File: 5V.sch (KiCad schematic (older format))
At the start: 11 parts

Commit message: LMZ13608 input caps
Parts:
- added C?: 10µ, Capacitors_SMD:C_1210, symbol Device:C
- added C?: 10µ, symbol Device:C
- C?: value 30µ -> 10µ; footprint (none) -> Capacitors_SMD:C_1210; Dielectric X5R/X7R -> X7R; MPN (none) -> GRM32ER71J106KA12L
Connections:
- net GND: now also C?.2, C?.2
- net VIN: now also C?.1, C?.1
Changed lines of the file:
@@
 	1    0    0    -1
 $EndComp
-Wire Wire Line
-	2650 2750 2800 2750
 NoConn ~ 3500 2700
 $Comp
@@
 P 2800 3000
 F 0 "C?" H 2915 3046 50  0000 L CNN
-F 1 "30µ" H 2915 2955 50  0000 L CNN
-F 2 "" H 2838 2850 50  0001 C CNN
+F 1 "10µ" H 2915 2955 50  0000 L CNN
+F 2 "Capacitors_SMD:C_1210" H 2838 2850 50  0001 C CNN
 F 3 "~" H 2800 3000 50  0001 C CNN
-F 4 "X5R/X7R" H 2800 3000 50  0001 C CNN "Dielectric"
+F 4 "X7R" H 2800 3000 50  0001 C CNN "Dielectric"
+F 5 "GRM32ER71J106KA12L" H 2800 3000 50  0001 C CNN "MPN"
 	1    2800 3000
 	1    0    0    -1
@@
 	1    0    0    -1
 $EndComp
-Wire Wire Line
-	2800 3250 2800 3150
 Text HLabel 5900 3300 1    50   Input ~ 0
 VIN
-Text HLabel 2650 2750 0    50   Input ~ 0
+Text HLabel 1950 2750 0    50   Input ~ 0
 VIN
 Text HLabel 5050 3750 0    50   Input ~ 0
@@
 	1    0    0    -1
 $EndComp
+$Comp
+L Device:C C?
+U 1 1 5C709529
+P 2450 3000
+F 0 "C?" H 2565 3046 50  0000 L CNN
+F 1 "10µ" H 2565 2955 50  0000 L CNN
+F 2 "Capacitors_SMD:C_1210" H 2488 2850 50  0001 C CNN
+F 3 "~" H 2450 3000 50  0001 C CNN
+F 4 "X7R" H 2450 3000 50  0001 C CNN "Dielectric"
+F 5 "GRM32ER71J106KA12L" H 2450 3000 50  0001 C CNN "MPN"
+	1    2450 3000
+	1    0    0    -1
+$EndComp
+$Comp
+L Device:C C?
+U 1 1 5C709573
+P 2100 3000
+F 0 "C?" H 2215 3046 50  0000 L CNN
+F 1 "10µ" H 2215 2955 50  0000 L CNN
+F 2 "" H 2138 2850 50  0001 C CNN
+F 3 "~" H 2100 3000 50  0001 C CNN
+F 4 "X7R" H 2100 3000 50  0001 C CNN "Dielectric"
+F 5 "GRM32ER71J106KA12L" H 2100 3000 50  0001 C CNN "MPN"
+	1    2100 3000
+	1    0    0    -1
+$EndComp
+Wire Wire Line
+	1950 2750 2100 2750
+Wire Wire Line
+	2100 2750 2100 2850
+Wire Wire Line
+	2100 2750 2450 2750
+Wire Wire Line
+	2450 2750 2450 2850
+Connection ~ 2100 2750
+Wire Wire Line
+	2450 2750 2800 2750
+Connection ~ 2450 2750
+Wire Wire Line
+	2100 3150 2100 3200
+Wire Wire Line
+	2100 3200 2450 3200
+Wire Wire Line
+	2800 3150 2800 3200
+Connection ~ 2800 3200
+Wire Wire Line
+	2800 3200 2800 3250
+Wire Wire Line
+	2450 3150 2450 3200
+Connection ~ 2450 3200
+Wire Wire Line
+	2450 3200 2800 3200
 $EndSCHEMATC

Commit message: fix missing footprint
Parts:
- C?: footprint (none) -> Capacitors_SMD:C_1210
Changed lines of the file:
@@
 F 0 "C?" H 2215 3046 50  0000 L CNN
 F 1 "10µ" H 2215 2955 50  0000 L CNN
-F 2 "" H 2138 2850 50  0001 C CNN
+F 2 "Capacitors_SMD:C_1210" H 2138 2850 50  0001 C CNN
 F 3 "~" H 2100 3000 50  0001 C CNN
 F 4 "X7R" H 2100 3000 50  0001 C CNN "Dielectric"

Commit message: LMZ13608 output caps
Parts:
- C? (x2): footprint (none) -> Capacitors_Tantalum_SMD:CP_Tantalum_Case-D_EIA-7343-31_Reflow; MPN (none) -> T520D337M006ATE015
- C?: footprint (none) -> Capacitors_SMD:C_1206; MPN (none) -> LMK316BJ476ML-T
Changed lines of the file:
@@
 F 0 "C?" H 4465 3046 50  0000 L CNN
 F 1 "330µ" H 4465 2955 50  0000 L CNN
-F 2 "" H 4388 2850 50  0001 C CNN
+F 2 "Capacitors_Tantalum_SMD:CP_Tantalum_Case-D_EIA-7343-31_Reflow" H 4388 2850 50  0001 C CNN
 F 3 "~" H 4350 3000 50  0001 C CNN
 F 4 "15m" H 4350 3000 50  0001 C CNN "ESR"
 F 5 "Tantalum Polymer" H 4350 3000 50  0001 C CNN "Type"
+F 6 "T520D337M006ATE015" H 4350 3000 50  0001 C CNN "MPN"
 	1    4350 3000
 	1    0    0    -1
@@
 F 0 "C?" H 4865 3046 50  0000 L CNN
 F 1 "330µ" H 4865 2955 50  0000 L CNN
-F 2 "" H 4788 2850 50  0001 C CNN
+F 2 "Capacitors_Tantalum_SMD:CP_Tantalum_Case-D_EIA-7343-31_Reflow" H 4788 2850 50  0001 C CNN
 F 3 "~" H 4750 3000 50  0001 C CNN
 F 4 "15m" H 4750 3000 50  0001 C CNN "ESR"
 F 5 "Tantalum Polymer" H 4750 3000 50  0001 C CNN "Type"
+F 6 "T520D337M006ATE015" H 4750 3000 50  0001 C CNN "MPN"
 	1    4750 3000
 	1    0    0    -1
@@
 F 0 "C?" H 5265 3046 50  0000 L CNN
 F 1 "47µ" H 5265 2955 50  0000 L CNN
-F 2 "" H 5188 2850 50  0001 C CNN
+F 2 "Capacitors_SMD:C_1206" H 5188 2850 50  0001 C CNN
 F 3 "~" H 5150 3000 50  0001 C CNN
 F 4 "X5R" H 5150 3000 50  0001 C CNN "Dielectric"
 F 5 "Ceramic" H 5150 3000 50  0001 C CNN "Type"
+F 6 "LMK316BJ476ML-T" H 5150 3000 50  0001 C CNN "MPN"
 	1    5150 3000
 	1    0    0    -1

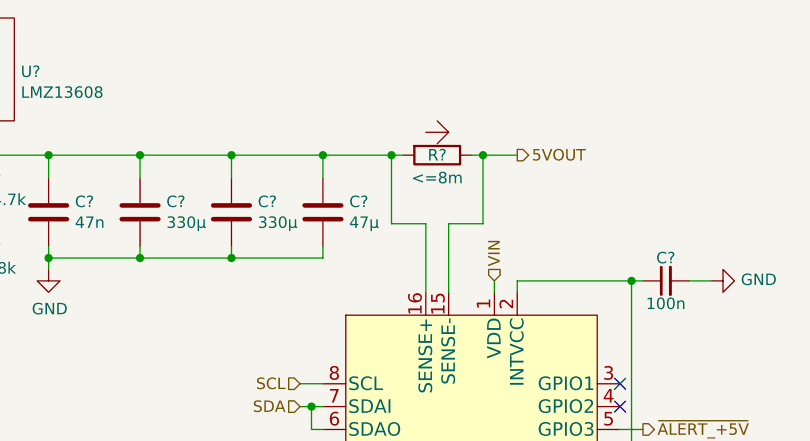
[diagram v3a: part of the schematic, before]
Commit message: 5V shunt
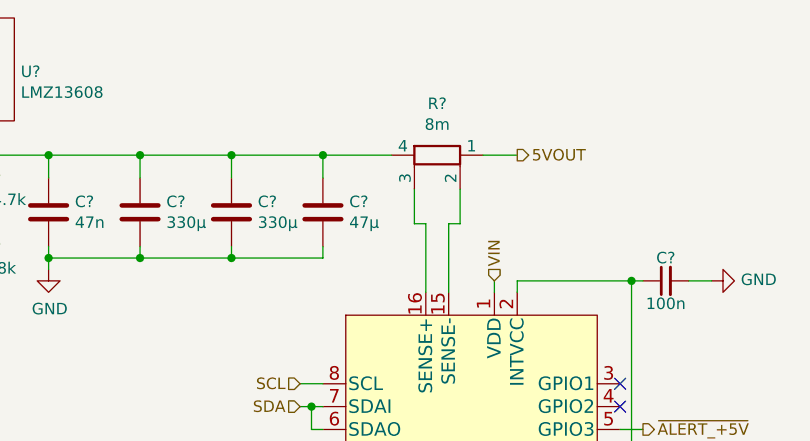
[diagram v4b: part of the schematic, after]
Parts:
- removed R?: <=8m, Resistor_SMD:R_2512_6332Metric, symbol shunt:R_Shunt
- added R?: 8m, ottojo_resistor:R_3637, symbol Device:R_Shunt
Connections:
- net 5VOUT: now also R?.1; no longer U?.15 (SENSE-)
- net at C?.1, C?.1, C?.1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: now also R?.4; no longer U?.16 (SENSE+)
- new net: R?.2, U?.15 (SENSE-)
- new net: R?.3, U?.16 (SENSE+)
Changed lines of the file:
@@
-$EndComp
-$Comp
-L shunt:R_Shunt R?
-U 1 1 5C2D1B44
-P 5650 2750
-F 0 "R?" V 5650 2750 50  0000 C CNN
-F 1 "<=8m" V 5750 2750 50  0000 C CNN
-F 2 "Resistor_SMD:R_2512_6332Metric" V 5580 2750 50  0001 C CNN
-F 3 "~" H 5650 2750 50  0001 C CNN
-F 4 ">2W" V 5650 2750 50  0001 C CNN "Power"
-	1    5650 2750
-	0    1    1    0
 $EndComp
 $Comp
@@
 Wire Wire Line
 	5150 2850 5150 2750
-Connection ~ 5150 2750
 Wire Wire Line
 	3950 3200 4350 3200
@@
 	3000 2750 3000 2700
 Wire Wire Line
-	5150 2750 5450 2750
-Wire Wire Line
-	5800 2750 5850 2750
-Wire Wire Line
 	5600 3350 5600 3050
 Wire Wire Line
-	5600 3050 5450 3050
-Wire Wire Line
-	5450 3050 5450 2750
-Connection ~ 5450 2750
-Wire Wire Line
-	5450 2750 5500 2750
-Wire Wire Line
-	5700 3050 5850 3050
-Wire Wire Line
-	5850 3050 5850 2750
-Connection ~ 5850 2750
-Wire Wire Line
-	5850 2750 6000 2750
+	5600 3050 5550 3050
+Wire Wire Line
+	5700 3050 5750 3050
 Wire Wire Line
 	5700 3050 5700 3350
@@
 Wire Wire Line
 	2450 3200 2800 3200
+$Comp
+L Device:R_Shunt R?
+U 1 1 5C722741
+P 5650 2750
+F 0 "R?" V 5425 2750 50  0000 C CNN
+F 1 "8m" V 5516 2750 50  0000 C CNN
+F 2 "ottojo_resistor:R_3637" V 5580 2750 50  0001 C CNN
+F 3 "~" H 5650 2750 50  0001 C CNN
+F 4 ">2W" V 5650 2750 50  0001 C CNN "Power"
+F 5 "WSL36378L000FEA" V 5650 2750 50  0001 C CNN "MPN"
+	1    5650 2750
+	0    1    1    0
+$EndComp
+Wire Wire Line
+	5550 3050 5550 2900
+Wire Wire Line
+	5750 2900 5750 3050
+Wire Wire Line
+	5850 2750 6000 2750
+Wire Wire Line
+	5450 2750 5150 2750
+Connection ~ 5150 2750
 $EndSCHEMATC

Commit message: fix footprints
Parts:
- C?: footprint Capacitors_SMD:C_1206 -> Capacitor_SMD:C_1206_3216Metric
- C? (x3): footprint Capacitors_SMD:C_1210 -> Capacitor_SMD:C_1210_3225Metric
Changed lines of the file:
@@
 F 0 "C?" H 5265 3046 50  0000 L CNN
 F 1 "47µ" H 5265 2955 50  0000 L CNN
-F 2 "Capacitors_SMD:C_1206" H 5188 2850 50  0001 C CNN
+F 2 "Capacitor_SMD:C_1206_3216Metric" H 5188 2850 50  0001 C CNN
 F 3 "~" H 5150 3000 50  0001 C CNN
 F 4 "X5R" H 5150 3000 50  0001 C CNN "Dielectric"
@@
 F 0 "C?" H 2915 3046 50  0000 L CNN
 F 1 "10µ" H 2915 2955 50  0000 L CNN
-F 2 "Capacitors_SMD:C_1210" H 2838 2850 50  0001 C CNN
+F 2 "Capacitor_SMD:C_1210_3225Metric" H 2838 2850 50  0001 C CNN
 F 3 "~" H 2800 3000 50  0001 C CNN
 F 4 "X7R" H 2800 3000 50  0001 C CNN "Dielectric"
@@
 F 0 "C?" H 2565 3046 50  0000 L CNN
 F 1 "10µ" H 2565 2955 50  0000 L CNN
-F 2 "Capacitors_SMD:C_1210" H 2488 2850 50  0001 C CNN
+F 2 "Capacitor_SMD:C_1210_3225Metric" H 2488 2850 50  0001 C CNN
 F 3 "~" H 2450 3000 50  0001 C CNN
 F 4 "X7R" H 2450 3000 50  0001 C CNN "Dielectric"
@@
 F 0 "C?" H 2215 3046 50  0000 L CNN
 F 1 "10µ" H 2215 2955 50  0000 L CNN
-F 2 "Capacitors_SMD:C_1210" H 2138 2850 50  0001 C CNN
+F 2 "Capacitor_SMD:C_1210_3225Metric" H 2138 2850 50  0001 C CNN
 F 3 "~" H 2100 3000 50  0001 C CNN
 F 4 "X7R" H 2100 3000 50  0001 C CNN "Dielectric"

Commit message: update footprints
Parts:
- C? (x2): footprint Capacitors_Tantalum_SMD:CP_Tantalum_Case-D_EIA-7343-31_Reflow -> Capacitor_Tantalum_SMD:CP_EIA-7343-31_Kemet-D
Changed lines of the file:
@@
 F 0 "C?" H 4465 3046 50  0000 L CNN
 F 1 "330µ" H 4465 2955 50  0000 L CNN
-F 2 "Capacitors_Tantalum_SMD:CP_Tantalum_Case-D_EIA-7343-31_Reflow" H 4388 2850 50  0001 C CNN
+F 2 "Capacitor_Tantalum_SMD:CP_EIA-7343-31_Kemet-D" H 4388 2850 50  0001 C CNN
 F 3 "~" H 4350 3000 50  0001 C CNN
 F 4 "15m" H 4350 3000 50  0001 C CNN "ESR"
@@
 F 0 "C?" H 4865 3046 50  0000 L CNN
 F 1 "330µ" H 4865 2955 50  0000 L CNN
-F 2 "Capacitors_Tantalum_SMD:CP_Tantalum_Case-D_EIA-7343-31_Reflow" H 4788 2850 50  0001 C CNN
+F 2 "Capacitor_Tantalum_SMD:CP_EIA-7343-31_Kemet-D" H 4788 2850 50  0001 C CNN
 F 3 "~" H 4750 3000 50  0001 C CNN
 F 4 "15m" H 4750 3000 50  0001 C CNN "ESR"

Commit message: smaller shunt on 5v rail
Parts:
- R?: footprint ottojo_resistor:R_3637 -> Resistor_SMD:R_2010_5025Metric; symbol Device:R_Shunt -> Device:R; MPN WSL36378L000FEA -> ERJ-MP3PF8M0U
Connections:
- net 5VOUT: now also U?.15 (SENSE-)
- net at C?.1, C?.1, C?.1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: now also R?.2, U?.16 (SENSE+); no longer R?.4
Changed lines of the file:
@@
 	5600 3350 5600 3050
-Wire Wire Line
-	5600 3050 5550 3050
-Wire Wire Line
-	5700 3050 5750 3050
 Wire Wire Line
 	5700 3050 5700 3350
@@
 	2450 3200 2800 3200
 $Comp
-L Device:R_Shunt R?
+L Device:R R?
 U 1 1 5C722741
 P 5650 2750
 F 0 "R?" V 5425 2750 50  0000 C CNN
 F 1 "8m" V 5516 2750 50  0000 C CNN
-F 2 "ottojo_resistor:R_3637" V 5580 2750 50  0001 C CNN
+F 2 "Resistor_SMD:R_2010_5025Metric" V 5580 2750 50  0001 C CNN
 F 3 "~" H 5650 2750 50  0001 C CNN
 F 4 ">2W" V 5650 2750 50  0001 C CNN "Power"
-F 5 "WSL36378L000FEA" V 5650 2750 50  0001 C CNN "MPN"
+F 5 "ERJ-MP3PF8M0U" V 5650 2750 50  0001 C CNN "MPN"
 	1    5650 2750
 	0    1    1    0
 $EndComp
+Connection ~ 5150 2750
 Wire Wire Line
-	5550 3050 5550 2900
+	5150 2750 5450 2750
 Wire Wire Line
-	5750 2900 5750 3050
+	5800 2750 5850 2750
+Wire Wire Line
+	5850 2750 5850 3050
+Connection ~ 5850 2750
 Wire Wire Line
 	5850 2750 6000 2750
 Wire Wire Line
-	5450 2750 5150 2750
-Connection ~ 5150 2750
+	5450 2750 5450 3050
+Connection ~ 5450 2750
+Wire Wire Line
+	5450 2750 5500 2750
+Wire Wire Line
+	5450 3050 5600 3050
+Wire Wire Line
+	5700 3050 5850 3050
 $EndSCHEMATC

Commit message: annotate parts
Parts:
- gave numbers to parts that had none: 13
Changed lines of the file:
@@
 $EndDescr
 $Comp
-L power:GND #PWR?
+L power:GND #PWR018
 U 1 1 5C2D1347
 P 6550 4350
-F 0 "#PWR?" H 6550 4100 50  0001 C CNN
+F 0 "#PWR018" H 6550 4100 50  0001 C CNN
 F 1 "GND" V 6555 4222 50  0000 R CNN
 F 2 "" H 6550 4350 50  0001 C CNN
@@
 $EndComp
 $Comp
-L Device:C_Small C?
+L Device:C_Small C18
 U 1 1 5C2D15AF
 P 6650 3300
-F 0 "C?" V 6750 3300 50  0000 C CNN
+F 0 "C18" V 6750 3300 50  0000 C CNN
 F 1 "100n" V 6550 3300 50  0000 C CNN
 F 2 "Capacitor_SMD:C_0603_1608Metric" H 6650 3300 50  0001 C CNN
@@
 $EndComp
 $Comp
-L power:GND #PWR?
+L power:GND #PWR019
 U 1 1 5C2D16C8
 P 6850 3300
-F 0 "#PWR?" H 6850 3050 50  0001 C CNN
+F 0 "#PWR019" H 6850 3050 50  0001 C CNN
 F 1 "GND" V 6855 3172 50  0000 R CNN
 F 2 "" H 6850 3300 50  0001 C CNN
@@
 $EndComp
 $Comp
-L LMZ13608:LMZ13608 U?
+L LMZ13608:LMZ13608 U2
 U 1 1 5C2D7DB3
 P 3300 2350
-F 0 "U?" H 3828 2315 50  0000 L CNN
+F 0 "U2" H 3828 2315 50  0000 L CNN
 F 1 "LMZ13608" H 3828 2224 50  0000 L CNN
 F 2 "LMZ13608:LMZ13608" H 3300 2350 50  0001 C CNN
@@
 Connection ~ 3300 2750
 $Comp
-L power:GND #PWR?
+L power:GND #PWR013
 U 1 1 5C2D92A7
 P 3300 2850
-F 0 "#PWR?" H 3300 2600 50  0001 C CNN
+F 0 "#PWR013" H 3300 2600 50  0001 C CNN
 F 1 "GND" H 3305 2677 50  0000 C CNN
 F 2 "" H 3300 2850 50  0001 C CNN
@@
 $EndComp
 $Comp
-L Device:R_Small R?
+L Device:R_Small R14
 U 1 1 5C2D93AE
 P 3600 2900
-F 0 "R?" H 3659 2946 50  0000 L CNN
+F 0 "R14" H 3659 2946 50  0000 L CNN
 F 1 "14.7k" H 3659 2855 50  0000 L CNN
 F 2 "Resistor_SMD:R_0603_1608Metric" H 3600 2900 50  0001 C CNN
@@
 $EndComp
 $Comp
-L Device:R_Small R?
+L Device:R_Small R15
 U 1 1 5C2D93E0
 P 3600 3200
-F 0 "R?" H 3659 3246 50  0000 L CNN
+F 0 "R15" H 3659 3246 50  0000 L CNN
 F 1 "2.8k" H 3659 3155 50  0000 L CNN
 F 2 "Resistor_SMD:R_0603_1608Metric" H 3600 3200 50  0001 C CNN
@@
 	3600 3300 3600 3400
 $Comp
-L power:GND #PWR?
+L power:GND #PWR014
 U 1 1 5C2DA3DE
 P 3600 3400
-F 0 "#PWR?" H 3600 3150 50  0001 C CNN
+F 0 "#PWR014" H 3600 3150 50  0001 C CNN
 F 1 "GND" H 3605 3227 50  0000 C CNN
 F 2 "" H 3600 3400 50  0001 C CNN
@@
 NoConn ~ 3500 2700
 $Comp
-L Device:C C?
+L Device:C C14
 U 1 1 5C2DC0D6
 P 3950 3000
-F 0 "C?" H 4065 3046 50  0000 L CNN
+F 0 "C14" H 4065 3046 50  0000 L CNN
 F 1 "47n" H 4065 2955 50  0000 L CNN
 F 2 "Capacitor_SMD:C_0603_1608Metric" H 3988 2850 50  0001 C CNN
@@
 	3950 3150 3950 3200
 $Comp
-L power:GND #PWR?
+L power:GND #PWR015
 U 1 1 5C2DD631
 P 3950 3250
-F 0 "#PWR?" H 3950 3000 50  0001 C CNN
+F 0 "#PWR015" H 3950 3000 50  0001 C CNN
 F 1 "GND" H 3955 3077 50  0000 C CNN
 F 2 "" H 3950 3250 50  0001 C CNN
@@
 $EndComp
 $Comp
-L Device:C C?
+L Device:C C15
 U 1 1 5C2DD6B4
 P 4350 3000
-F 0 "C?" H 4465 3046 50  0000 L CNN
+F 0 "C15" H 4465 3046 50  0000 L CNN
 F 1 "330µ" H 4465 2955 50  0000 L CNN
 F 2 "Capacitor_Tantalum_SMD:CP_EIA-7343-31_Kemet-D" H 4388 2850 50  0001 C CNN
@@
 $EndComp
 $Comp
-L Device:C C?
+L Device:C C16
 U 1 1 5C2DDE4E
 P 4750 3000
-F 0 "C?" H 4865 3046 50  0000 L CNN
+F 0 "C16" H 4865 3046 50  0000 L CNN
 F 1 "330µ" H 4865 2955 50  0000 L CNN
 F 2 "Capacitor_Tantalum_SMD:CP_EIA-7343-31_Kemet-D" H 4788 2850 50  0001 C CNN
@@
 $EndComp
 $Comp
-L Device:C C?
+L Device:C C17
 U 1 1 5C2DDE91
 P 5150 3000
-F 0 "C?" H 5265 3046 50  0000 L CNN
+F 0 "C17" H 5265 3046 50  0000 L CNN
 F 1 "47µ" H 5265 2955 50  0000 L CNN
 F 2 "Capacitor_SMD:C_1206_3216Metric" H 5188 2850 50  0001 C CNN
@@
 	4350 3200 4750 3200
 $Comp
-L Device:C C?
+L Device:C C13
 U 1 1 5C2E1567
 P 2800 3000
-F 0 "C?" H 2915 3046 50  0000 L CNN
+F 0 "C13" H 2915 3046 50  0000 L CNN
 F 1 "10µ" H 2915 2955 50  0000 L CNN
 F 2 "Capacitor_SMD:C_1210_3225Metric" H 2838 2850 50  0001 C CNN
@@
 	2800 2750 3000 2750
 $Comp
-L power:GND #PWR?
+L power:GND #PWR012
 U 1 1 5C2E20F7
 P 2800 3250
-F 0 "#PWR?" H 2800 3000 50  0001 C CNN
+F 0 "#PWR012" H 2800 3000 50  0001 C CNN
 F 1 "GND" H 2805 3077 50  0000 C CNN
 F 2 "" H 2800 3250 50  0001 C CNN
@@
 	5150 4150 5050 4150
 $Comp
-L power:GND #PWR?
+L power:GND #PWR016
 U 1 1 5C370C74
 P 5050 4150
-F 0 "#PWR?" H 5050 3900 50  0001 C CNN
+F 0 "#PWR016" H 5050 3900 50  0001 C CNN
 F 1 "GND" V 5055 4022 50  0000 R CNN
 F 2 "" H 5050 4150 50  0001 C CNN
@@
 $EndComp
 $Comp
-L power:GND #PWR?
+L power:GND #PWR017
 U 1 1 5C370DDF
 P 5800 4850
-F 0 "#PWR?" H 5800 4600 50  0001 C CNN
+F 0 "#PWR017" H 5800 4600 50  0001 C CNN
 F 1 "GND" V 5805 4722 50  0000 R CNN
 F 2 "" H 5800 4850 50  0001 C CNN
@@
 NoConn ~ 6450 4150
 $Comp
-L LTC2946:LTC2946 U?
+L LTC2946:LTC2946 U3
 U 1 1 5C32FA1C
 P 5800 4050
-F 0 "U?" H 6300 3400 60  0000 C CNN
+F 0 "U3" H 6300 3400 60  0000 C CNN
 F 1 "LTC2946" H 5800 4000 60  0000 C CNN
 F 2 "Package_SO:MSOP-16_3x4mm_P0.5mm" H 6250 3200 60  0001 C CNN
@@
 $EndComp
 $Comp
-L Device:C C?
+L Device:C C12
 U 1 1 5C709529
 P 2450 3000
-F 0 "C?" H 2565 3046 50  0000 L CNN
+F 0 "C12" H 2565 3046 50  0000 L CNN
 F 1 "10µ" H 2565 2955 50  0000 L CNN
 F 2 "Capacitor_SMD:C_1210_3225Metric" H 2488 2850 50  0001 C CNN
@@
 $EndComp
 $Comp
-L Device:C C?
+L Device:C C11
 U 1 1 5C709573
 P 2100 3000
-F 0 "C?" H 2215 3046 50  0000 L CNN
+F 0 "C11" H 2215 3046 50  0000 L CNN
 F 1 "10µ" H 2215 2955 50  0000 L CNN
 F 2 "Capacitor_SMD:C_1210_3225Metric" H 2138 2850 50  0001 C CNN
@@
 	2450 3200 2800 3200
 $Comp
-L Device:R R?
+L Device:R R16
 U 1 1 5C722741
 P 5650 2750
-F 0 "R?" V 5425 2750 50  0000 C CNN
+F 0 "R16" V 5425 2750 50  0000 C CNN
 F 1 "8m" V 5516 2750 50  0000 C CNN
 F 2 "Resistor_SMD:R_2010_5025Metric" V 5580 2750 50  0001 C CNN
